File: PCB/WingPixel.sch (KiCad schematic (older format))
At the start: 16 parts, among them J1 Barrel_Jack, J2 Screw_Terminal_01x04, J3 Conn_01x16, J4 Conn_01x12, J5 TriSolderJumper, J6 Conn_01x02, SW1 SW_Push, U1 WingPixel, U2 LSF0102DCUR

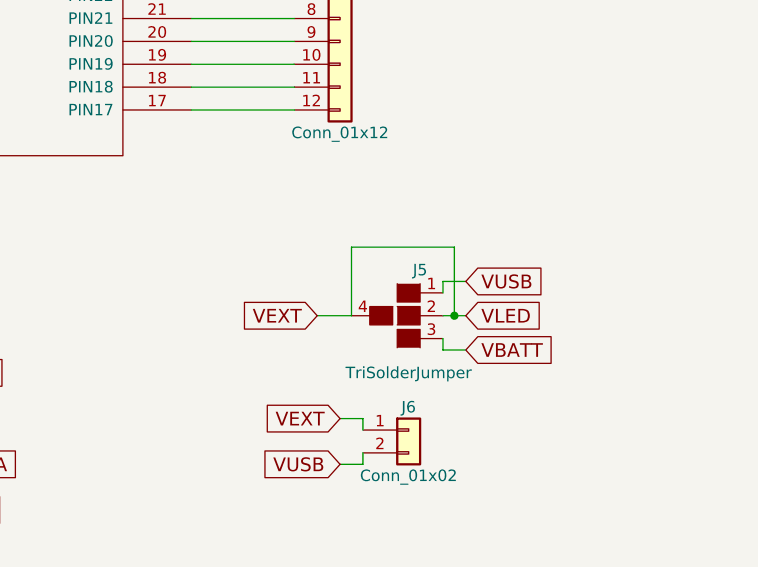
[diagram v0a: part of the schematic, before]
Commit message: Changing power distribution
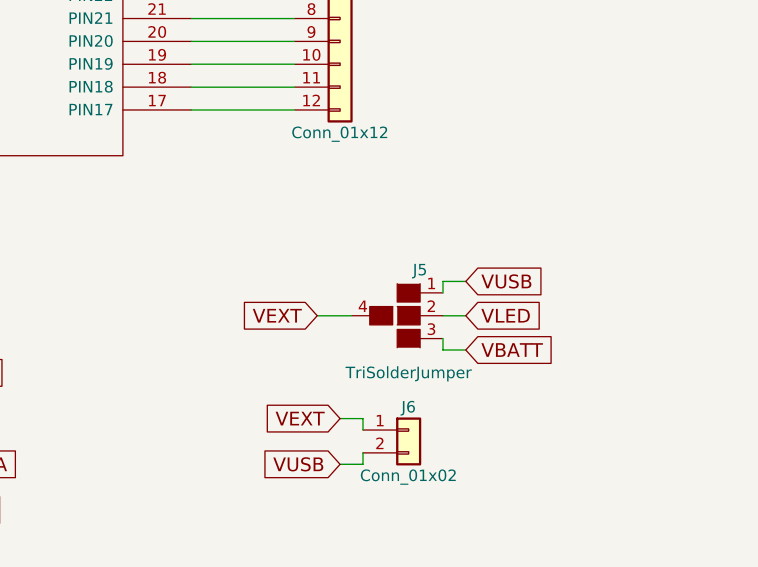
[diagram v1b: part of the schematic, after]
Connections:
- net +5V: no longer C1.1, J2.1 (Pin_1), J5.2 (1), R1.2, R4.2, R5.2, U2.7 (VCCB)
- new net VLED: C1.1, J2.1 (Pin_1), J5.2 (1), R1.2, R4.2, R5.2, U2.7 (VCCB)
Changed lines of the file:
@@
 Text GLabel 6000 4150 2    60   Input ~ 0
 VBATT
-Wire Wire Line
-	2750 3850 2750 4250
-Wire Wire Line
-	3050 4050 3250 4050
-Wire Wire Line
-	3050 4050 3050 4450
-Wire Wire Line
-	2850 1700 3300 1700
-Wire Wire Line
-	1700 4650 2250 4650
-Wire Wire Line
-	2100 4550 2100 4650
-Connection ~ 2100 4650
-Wire Wire Line
-	1700 4850 2250 4850
-Wire Wire Line
-	1900 4550 1900 4850
-Connection ~ 1900 4850
-Wire Wire Line
-	2550 4050 2550 4250
-Wire Wire Line
-	1800 4050 2550 4050
-Wire Wire Line
-	1900 4250 1900 4050
-Connection ~ 1900 4050
-Wire Wire Line
-	2100 4250 2100 4050
-Connection ~ 2100 4050
-Wire Wire Line
-	3550 4050 3650 4050
-Wire Wire Line
-	3050 4650 3700 4650
-Wire Wire Line
-	3050 4850 3700 4850
-Wire Wire Line
-	3250 4600 3250 4650
-Connection ~ 3250 4650
-Wire Wire Line
-	3450 4600 3450 4850
-Connection ~ 3450 4850
-Wire Wire Line
-	3250 4250 3650 4250
-Wire Wire Line
-	3250 4250 3250 4300
-Wire Wire Line
-	3450 4250 3450 4300
-Connection ~ 3450 4250
-Connection ~ 2750 4050
-Wire Wire Line
-	2800 3850 2750 3850
-Wire Wire Line
-	5950 1250 6050 1250
-Wire Wire Line
-	6050 1250 6050 1350
-Wire Wire Line
-	6050 1650 6050 1750
-Wire Wire Line
-	6050 1750 6150 1750
-Wire Wire Line
-	6400 2000 6500 2000
-Wire Wire Line
-	6400 2100 6500 2100
-Wire Wire Line
-	6400 2200 6500 2200
-Wire Wire Line
-	6400 2300 6500 2300
-Wire Wire Line
-	2850 2600 3300 2600
-Wire Wire Line
-	2850 2700 3300 2700
-Wire Wire Line
-	3250 2600 3250 3400
-Wire Wire Line
-	3250 3400 3500 3400
-Connection ~ 3250 2600
-Wire Wire Line
-	3150 3550 3150 2700
-Connection ~ 3150 2700
-Wire Wire Line
-	4800 2000 5250 2000
-Wire Wire Line
-	5250 2100 4800 2100
-Wire Wire Line
-	4800 2200 5250 2200
-Wire Wire Line
-	4900 1650 5200 1650
-Wire Wire Line
-	5150 1650 5150 2000
-Connection ~ 5150 2000
-Wire Wire Line
-	5200 1500 5050 1500
-Connection ~ 5050 2200
-Wire Wire Line
-	2100 1200 1950 1200
-Wire Wire Line
-	1950 1200 1950 1100
-Wire Wire Line
-	2100 1000 1950 1000
-Wire Wire Line
-	3150 3550 3500 3550
-Wire Wire Line
-	3300 1600 2850 1600
-Wire Wire Line
-	3300 1800 2850 1800
-Wire Wire Line
-	3300 1900 2850 1900
-Wire Wire Line
-	2850 1350 2900 1350
-Wire Wire Line
-	2900 1350 2900 1600
-Connection ~ 2900 1600
-Wire Wire Line
-	2850 1200 3250 1200
-Wire Wire Line
-	3000 1200 3000 1700
-Connection ~ 3000 1700
-Wire Wire Line
-	2850 1050 3100 1050
-Wire Wire Line
-	3100 1050 3100 1900
-Connection ~ 3100 1900
-Wire Wire Line
-	3300 2000 2850 2000
-Wire Wire Line
-	2850 2100 3300 2100
-Wire Wire Line
-	3300 2200 2850 2200
-Wire Wire Line
-	2850 2300 3300 2300
-Wire Wire Line
-	3300 2400 2850 2400
-Wire Wire Line
-	2850 2500 3300 2500
-Wire Wire Line
-	3300 2800 2850 2800
-Wire Wire Line
-	2850 2900 3300 2900
-Wire Wire Line
-	3300 3000 2850 3000
-Wire Wire Line
-	2850 3100 3300 3100
-Wire Wire Line
-	4800 3100 5250 3100
-Wire Wire Line
-	5250 3000 4800 3000
-Wire Wire Line
-	4800 2900 5250 2900
-Wire Wire Line
-	5250 2800 4800 2800
-Wire Wire Line
-	4800 2700 5250 2700
-Wire Wire Line
-	5250 2600 4800 2600
-Wire Wire Line
-	4800 2500 5250 2500
-Wire Wire Line
-	5250 2400 4800 2400
-Wire Wire Line
-	4800 2300 5250 2300
-Wire Wire Line
-	6000 4150 5900 4150
-Wire Wire Line
-	5900 4150 5900 4100
 $Comp
 L TriSolderJumper J5
@@
 Text GLabel 2750 5350 2    60   Input ~ 0
 GND
-Wire Wire Line
-	2650 5250 2650 5350
-Wire Wire Line
-	2650 5350 2750 5350
 $Comp
 L +5V #PWR01
@@
 	1    0    0    -1
 $EndComp
-Wire Wire Line
-	2050 900  2050 1000
-Connection ~ 2050 1000
 $Comp
 L GND #PWR02
@@
 	1    0    0    -1
 $EndComp
-Wire Wire Line
-	2050 1300 2050 1200
-Connection ~ 2050 1200
 $Comp
 L +3.3V #PWR03
@@
 	1    0    0    -1
 $EndComp
-Connection ~ 3000 1200
 $Comp
 L +BATT #PWR04
@@
 	1    0    0    -1
 $EndComp
-Connection ~ 5150 1650
-Wire Wire Line
-	5900 4000 6000 4000
 Text GLabel 5350 4000 0    60   Input ~ 0
 VEXT
-Wire Wire Line
-	5500 4000 5350 4000
 Text GLabel 6000 3850 2    60   Input ~ 0
 VUSB
-Wire Wire Line
-	6000 3850 5900 3850
-Wire Wire Line
-	5900 3850 5900 3900
 $Comp
 L Conn_01x02 J6
@@
 Text GLabel 5450 4450 0    60   Input ~ 0
 VEXT
-Wire Wire Line
-	5450 4450 5550 4450
-Wire Wire Line
-	5550 4450 5550 4500
 $Comp
 L SW_Push SW1
@@
 	1    0    0    -1
 $EndComp
-Wire Wire Line
-	1050 2500 1150 2500
-Wire Wire Line
-	1550 2500 1700 2500
 Text GLabel 5450 4650 0    60   Input ~ 0
 VUSB
 Wire Wire Line
+	2750 3850 2750 4250
+Wire Wire Line
+	3050 4050 3250 4050
+Wire Wire Line
+	3050 4050 3050 4450
+Wire Wire Line
+	2850 1700 3300 1700
+Wire Wire Line
+	1700 4650 2250 4650
+Wire Wire Line
+	2100 4550 2100 4650
+Connection ~ 2100 4650
+Wire Wire Line
+	1700 4850 2250 4850
+Wire Wire Line
+	1900 4550 1900 4850
+Connection ~ 1900 4850
+Wire Wire Line
+	2550 4050 2550 4250
+Wire Wire Line
+	1800 4050 2550 4050
+Wire Wire Line
+	1900 4250 1900 4050
+Connection ~ 1900 4050
+Wire Wire Line
+	2100 4250 2100 4050
+Connection ~ 2100 4050
+Wire Wire Line
+	3550 4050 3650 4050
+Wire Wire Line
+	3050 4650 3700 4650
+Wire Wire Line
+	3050 4850 3700 4850
+Wire Wire Line
+	3250 4600 3250 4650
+Connection ~ 3250 4650
+Wire Wire Line
+	3450 4600 3450 4850
+Connection ~ 3450 4850
+Wire Wire Line
+	3250 4250 3650 4250
+Wire Wire Line
+	3250 4250 3250 4300
+Wire Wire Line
+	3450 4250 3450 4300
+Connection ~ 3450 4250
+Connection ~ 2750 4050
+Wire Wire Line
+	2800 3850 2750 3850
+Wire Wire Line
+	5950 1250 6050 1250
+Wire Wire Line
+	6050 1250 6050 1350
+Wire Wire Line
+	6050 1650 6050 1750
+Wire Wire Line
+	6050 1750 6150 1750
+Wire Wire Line
+	6400 2000 6500 2000
+Wire Wire Line
+	6400 2100 6500 2100
+Wire Wire Line
+	6400 2200 6500 2200
+Wire Wire Line
+	6400 2300 6500 2300
+Wire Wire Line
+	2850 2600 3300 2600
+Wire Wire Line
+	2850 2700 3300 2700
+Wire Wire Line
+	3250 2600 3250 3400
+Wire Wire Line
+	3250 3400 3500 3400
+Connection ~ 3250 2600
+Wire Wire Line
+	3150 3550 3150 2700
+Connection ~ 3150 2700
+Wire Wire Line
+	4800 2000 5250 2000
+Wire Wire Line
+	5250 2100 4800 2100
+Wire Wire Line
+	4800 2200 5250 2200
+Wire Wire Line
+	4900 1650 5200 1650
+Wire Wire Line
+	5150 1650 5150 2000
+Connection ~ 5150 2000
+Wire Wire Line
+	5200 1500 5050 1500
+Connection ~ 5050 2200
+Wire Wire Line
+	2100 1200 1950 1200
+Wire Wire Line
+	1950 1200 1950 1100
+Wire Wire Line
+	2100 1000 1950 1000
+Wire Wire Line
+	3150 3550 3500 3550
+Wire Wire Line
+	3300 1600 2850 1600
+Wire Wire Line
+	3300 1800 2850 1800
+Wire Wire Line
+	3300 1900 2850 1900
+Wire Wire Line
+	2850 1350 2900 1350
+Wire Wire Line
+	2900 1350 2900 1600
+Connection ~ 2900 1600
+Wire Wire Line
+	2850 1200 3250 1200
+Wire Wire Line
+	3000 1200 3000 1700
+Connection ~ 3000 1700
+Wire Wire Line
+	2850 1050 3100 1050
+Wire Wire Line
+	3100 1050 3100 1900
+Connection ~ 3100 1900
+Wire Wire Line
+	3300 2000 2850 2000
+Wire Wire Line
+	2850 2100 3300 2100
+Wire Wire Line
+	3300 2200 2850 2200
+Wire Wire Line
+	2850 2300 3300 2300
+Wire Wire Line
+	3300 2400 2850 2400
+Wire Wire Line
+	2850 2500 3300 2500
+Wire Wire Line
+	3300 2800 2850 2800
+Wire Wire Line
+	2850 2900 3300 2900
+Wire Wire Line
+	3300 3000 2850 3000
+Wire Wire Line
+	2850 3100 3300 3100
+Wire Wire Line
+	4800 3100 5250 3100
+Wire Wire Line
+	5250 3000 4800 3000
+Wire Wire Line
+	4800 2900 5250 2900
+Wire Wire Line
+	5250 2800 4800 2800
+Wire Wire Line
+	4800 2700 5250 2700
+Wire Wire Line
+	5250 2600 4800 2600
+Wire Wire Line
+	4800 2500 5250 2500
+Wire Wire Line
+	5250 2400 4800 2400
+Wire Wire Line
+	4800 2300 5250 2300
+Wire Wire Line
+	6000 4150 5900 4150
+Wire Wire Line
+	5900 4150 5900 4100
+Wire Wire Line
+	2650 5250 2650 5350
+Wire Wire Line
+	2650 5350 2750 5350
+Wire Wire Line
+	2050 900  2050 1000
+Connection ~ 2050 1000
+Wire Wire Line
+	2050 1300 2050 1200
+Connection ~ 2050 1200
+Connection ~ 3000 1200
+Connection ~ 5150 1650
+Wire Wire Line
+	5900 4000 6000 4000
+Wire Wire Line
+	5500 4000 5350 4000
+Wire Wire Line
+	6000 3850 5900 3850
+Wire Wire Line
+	5900 3850 5900 3900
+Wire Wire Line
+	5450 4450 5550 4450
+Wire Wire Line
+	5550 4450 5550 4500
+Wire Wire Line
+	1050 2500 1150 2500
+Wire Wire Line
+	1550 2500 1700 2500
+Wire Wire Line
 	5450 4650 5550 4650
 Wire Wire Line
@@
 Wire Wire Line
 	5050 1500 5050 2200
-Wire Wire Line
-	5500 4000 5500 3700
-Wire Wire Line
-	5500 3700 5950 3700
-Wire Wire Line
-	5950 3700 5950 4000
-Connection ~ 5950 4000
 $EndSCHEMATC

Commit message: Saved Project, Sch, and PCB
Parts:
- J5: footprint TriSelectSolderJumper:TriSelectSolderJumper_CutTrace -> TriSelectSolderJumper:TriSelectSolderJumper_HighCurrent
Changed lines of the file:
@@
 F 0 "J5" H 5800 4200 50  0000 C CNN
 F 1 "TriSolderJumper" H 5750 3750 50  0000 C CNN
-F 2 "TriSelectSolderJumper:TriSelectSolderJumper_CutTrace" H 5750 3705 50  0001 C CNN
+F 2 "TriSelectSolderJumper:TriSelectSolderJumper_HighCurrent" H 5750 3705 50  0001 C CNN
 F 3 "" H 5750 4000 50  0001 C CNN
 	1    5750 4000

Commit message: Cleaned up Silk Screen, Added Labels and Logos
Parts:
- U1: footprint FeatherWing:FeatherWing -> FeatherWing:FeatherWing_NoOutline
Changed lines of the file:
@@
 F 0 "U1" H 4400 3350 50  0000 C CNN
 F 1 "WingPixel" H 4050 3350 50  0000 C CNN
-F 2 "FeatherWing:FeatherWing" H 4050 2350 50  0001 C CNN
+F 2 "FeatherWing:FeatherWing_NoOutline" H 4050 2350 50  0001 C CNN
 F 3 "DOCUMENTATION" H 4050 2350 50  0001 C CNN
 	1    4050 2350

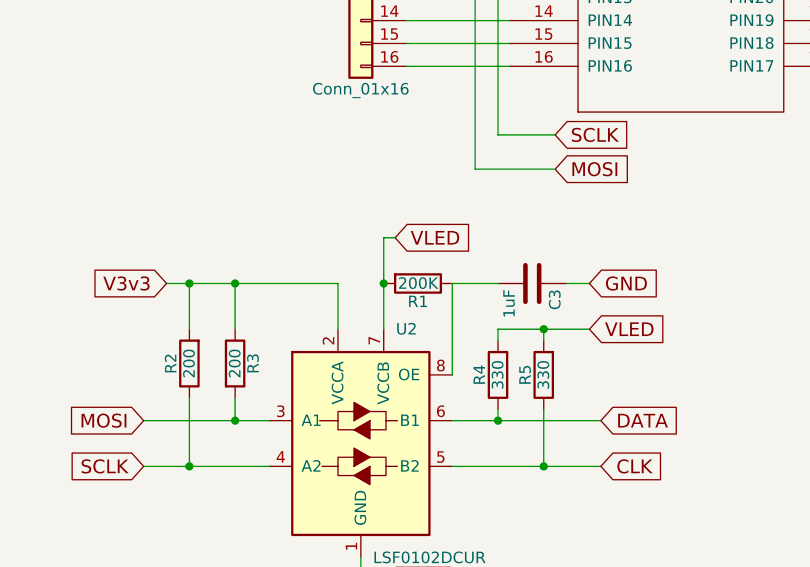
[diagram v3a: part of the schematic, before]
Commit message: Final PCB cleanup, fixed LvlShft wiring.
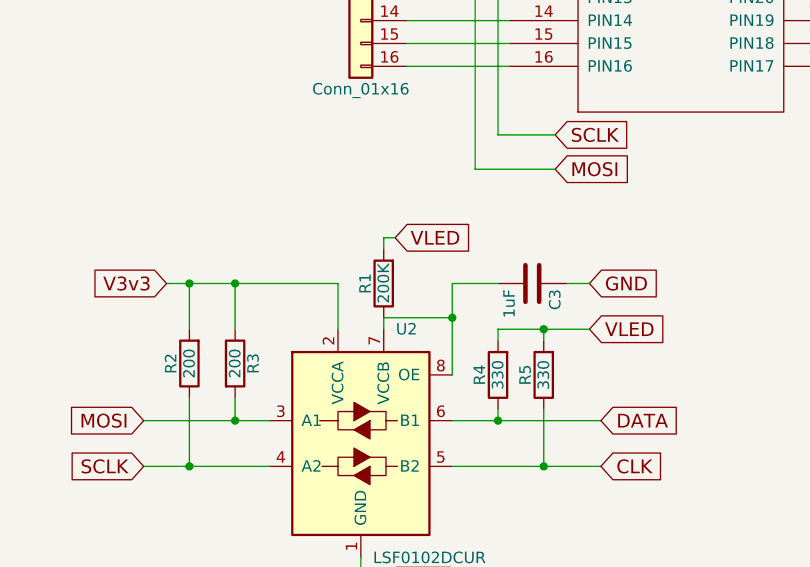
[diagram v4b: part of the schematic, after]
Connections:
- net VLED: no longer U2.7 (VCCB)
- net at C3.2, R1.1, U2.8 (OE): now also U2.7 (VCCB)
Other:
- moved on the sheet: R1
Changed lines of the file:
@@
 L R R1
 U 1 1 5A9AD929
-P 2900 4050
-F 0 "R1" V 2980 4050 50  0000 C CNN
-F 1 "200K" V 2900 4050 50  0000 C CNN
-F 2 "Resistors_SMD:R_0603" V 2830 4050 50  0001 C CNN
-F 3 "ERJ-3GEYJ331V" H 2900 4050 50  0001 C CNN
-	1    2900 4050
-	0    1    1    0
+P 2750 4050
+F 0 "R1" V 2830 4050 50  0000 C CNN
+F 1 "200K" V 2750 4050 50  0000 C CNN
+F 2 "Resistors_SMD:R_0603" V 2680 4050 50  0001 C CNN
+F 3 "ERJ-3GEYJ331V" H 2750 4050 50  0001 C CNN
+	1    2750 4050
+	-1   0    0    1
 $EndComp
 $Comp
@@
 VUSB
 Wire Wire Line
-	2750 3850 2750 4250
-Wire Wire Line
 	3050 4050 3250 4050
 Wire Wire Line
@@
 	3450 4250 3450 4300
 Connection ~ 3450 4250
-Connection ~ 2750 4050
-Wire Wire Line
-	2800 3850 2750 3850
 Wire Wire Line
 	5950 1250 6050 1250
@@
 Wire Wire Line
 	5050 1500 5050 2200
+Wire Wire Line
+	2800 3850 2750 3850
+Wire Wire Line
+	2750 3850 2750 3900
+Wire Wire Line
+	2750 4200 2750 4250
+Wire Wire Line
+	2750 4200 3050 4200
+Connection ~ 3050 4200
 $EndSCHEMATC

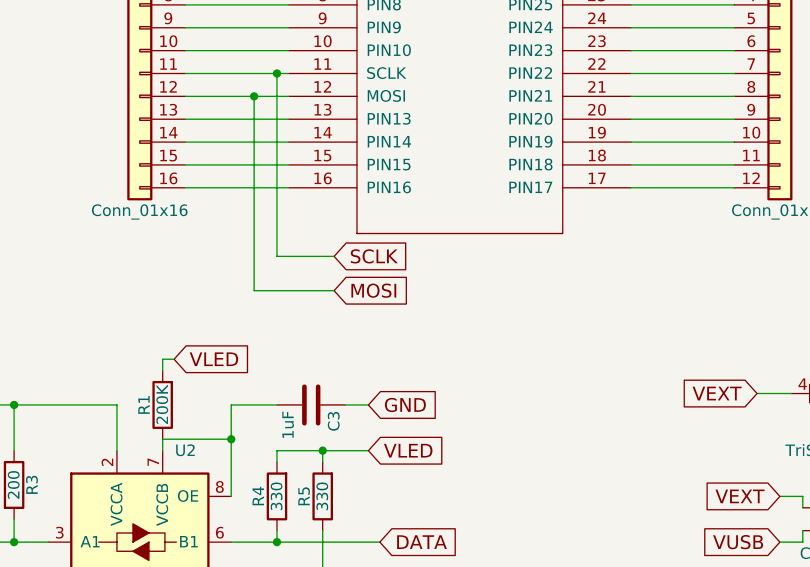
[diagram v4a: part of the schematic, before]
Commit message: Added placeholders for cuttable traces
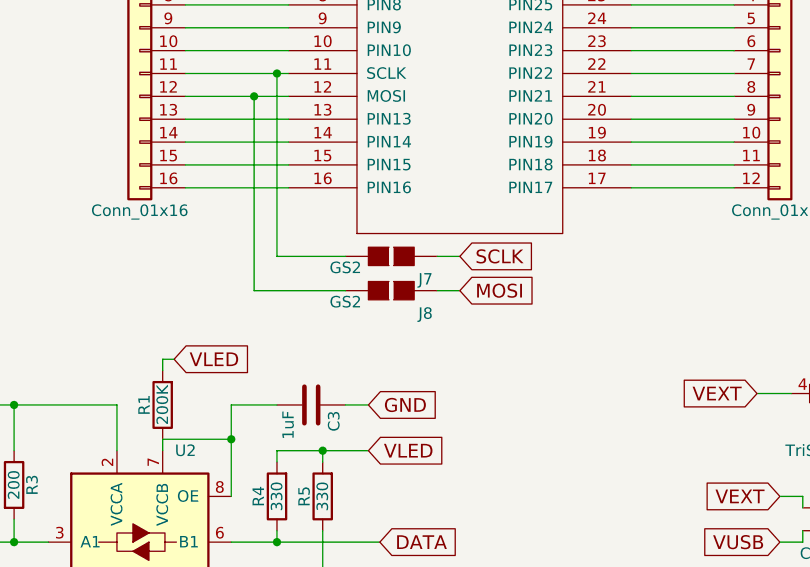
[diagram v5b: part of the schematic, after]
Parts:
- added J7, J8: GS2, Connectors:GS2, symbol GS2
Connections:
- net MOSI: now also J8.1 (G1); no longer J3.12 (Pin_12), U1.12 (MOSI)
- net SCLK: now also J7.1 (G1); no longer J3.11 (Pin_11), U1.11 (SCLK)
- new net: J3.11 (Pin_11), J7.2 (G2), U1.11 (SCLK)
- new net: J3.12 (Pin_12), J8.2 (G2), U1.12 (MOSI)
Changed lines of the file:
@@
 Text GLabel 3700 4650 2    60   Input ~ 0
 DATA
-Text GLabel 3500 3400 2    60   Input ~ 0
+Text GLabel 4050 3400 2    60   Input ~ 0
 SCLK
-Text GLabel 3500 3550 2    60   Input ~ 0
+Text GLabel 4050 3550 2    60   Input ~ 0
 MOSI
 Text GLabel 1700 4850 0    60   Input ~ 0
@@
 	3250 2600 3250 3400
 Wire Wire Line
-	3250 3400 3500 3400
+	3250 3400 3550 3400
 Connection ~ 3250 2600
 Wire Wire Line
@@
 	2100 1000 1950 1000
 Wire Wire Line
-	3150 3550 3500 3550
+	3150 3550 3550 3550
 Wire Wire Line
 	3300 1600 2850 1600
@@
 	2750 4200 3050 4200
 Connection ~ 3050 4200
+$Comp
+L GS2 J7
+U 1 1 5B26FA07
+P 3750 3400
+F 0 "J7" V 3850 3550 50  0000 C CNN
+F 1 "GS2" V 3800 3200 50  0000 C CNN
+F 2 "Connectors:GS2" V 3824 3400 50  0001 C CNN
+F 3 "" H 3750 3400 50  0001 C CNN
+	1    3750 3400
+	0    1    1    0
+$EndComp
+$Comp
+L GS2 J8
+U 1 1 5B26FAFC
+P 3750 3550
+F 0 "J8" V 3850 3700 50  0000 C CNN
+F 1 "GS2" V 3800 3350 50  0000 C CNN
+F 2 "Connectors:GS2" V 3824 3550 50  0001 C CNN
+F 3 "" H 3750 3550 50  0001 C CNN
+	1    3750 3550
+	0    1    1    0
+$EndComp
+Wire Wire Line
+	3950 3400 4050 3400
+Wire Wire Line
+	3950 3550 4050 3550
 $EndSCHEMATC

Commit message: Added Cut Trace footprints, moved cap and logo.
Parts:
- J7, J8: footprint Connectors:GS2 -> ML_CutTrace:2-PinCutTrace
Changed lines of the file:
@@
 F 0 "J7" V 3850 3550 50  0000 C CNN
 F 1 "GS2" V 3800 3200 50  0000 C CNN
-F 2 "Connectors:GS2" V 3824 3400 50  0001 C CNN
+F 2 "ML_CutTrace:2-PinCutTrace" V 3824 3400 50  0001 C CNN
 F 3 "" H 3750 3400 50  0001 C CNN
 	1    3750 3400
@@
 F 0 "J8" V 3850 3700 50  0000 C CNN
 F 1 "GS2" V 3800 3350 50  0000 C CNN
-F 2 "Connectors:GS2" V 3824 3550 50  0001 C CNN
+F 2 "ML_CutTrace:2-PinCutTrace" V 3824 3550 50  0001 C CNN
 F 3 "" H 3750 3550 50  0001 C CNN
 	1    3750 3550
